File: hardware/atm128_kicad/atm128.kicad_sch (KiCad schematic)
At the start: 57 parts, among them J1 Power Jack, J2 Conn_02x16_Odd_Even, J3 Conn_02x16_Odd_Even, J4 ISP, J5 JTAG, J6 USB_B_Mini, U1 LM2596S-5, U2 ATmega128-16A, U3 CH340G, Y1 Crystal

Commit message: feat: update hw: USB_C, IDC ISP, CH340E
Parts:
- removed C10, C11, C14: 1uF, Capacitor_SMD:C_0805_2012Metric, symbol Device:C
- removed C12: 10nF, Capacitor_SMD:C_0805_2012Metric, symbol Device:C
- removed C13: 100nF, Capacitor_SMD:C_0805_2012Metric, symbol Device:C
- removed D8: RX, LED_SMD:LED_0805_2012Metric, symbol Device:LED
- removed J4: ISP, Connector_PinHeader_2.54mm:PinHeader_1x06_P2.54mm_Vertical, symbol Connector_Generic:Conn_01x06
- removed J6: USB_B_Mini, Connector_USB:USB_Micro-B_Molex-105017-0001, symbol Connector:USB_B_Mini
- removed R11, R14, R15: 1k, Resistor_SMD:R_0805_2012Metric, symbol Device:R
- removed TP3: 5V, TestPoint:TestPoint_Pad_D1.0mm, symbol Connector:TestPoint
- removed U3: CH340G, Package_SO:SOIC-16_3.9x9.9mm_P1.27mm, symbol Interface_USB:CH340G
- removed Y1: Crystal, Crystal:Crystal_SMD_5032-2Pin_5.0x3.2mm, symbol Device:Crystal
- added C15: 10nF, Capacitor_SMD:C_0805_2012Metric, symbol Device:C
- added C16: 1uF, Capacitor_SMD:C_0805_2012Metric, symbol Device:C
- added C17: 100nF, Capacitor_SMD:C_0805_2012Metric, symbol Device:C
- added J4: ISP, Connector_IDC:IDC-Header_2x05_P2.54mm_Vertical, symbol Connector:AVR-ISP-10
- added J6: USB_C_Receptacle_USB2.0, Connector_USB:USB_C_Receptacle_HRO_TYPE-C-31-M-12, symbol Connector:USB_C_Receptacle_USB2.0
- added R16, R17: 5.1k, Resistor_SMD:R_0805_2012Metric, symbol Device:R
- added R18, R19: 1k, Resistor_SMD:R_0805_2012Metric, symbol Device:R
- added U4: CH340E, Package_SO:MSOP-10_3x3mm_P0.5mm, symbol Interface_USB:CH340E
- D7: value TX -> PROG
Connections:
- net +5V: now also C16.2, J4.2 (VCC), J6.A4 (VBUS), J6.A9 (VBUS), J6.B4 (VBUS), J6.B9 (VBUS), U4.7 (VCC)
- net CH_RX: now also R19.2, U4.9 (RXD)
- net CH_TX: now also R18.2, U4.8 (TXD)
- net GND: now also C15.1, C16.1, J4.10 (GND), J4.4 (GND), J4.6 (GND), J4.8 (GND), J6.A1 (GND), J6.A12 (GND), J6.B1 (GND), J6.B12 (GND), J6.S1 (SHIELD), R16.2, R17.2, U4.3 (GND)
- net RXD0: now also J4.1 (MOSI)
- net RXD1: now also R18.1
- net SPI_SCK: now also J4.7 (SCK)
- net TXD0: now also J4.9 (MISO)
- net TXD1: now also R19.1
- net USB_D+: now also J6.A6 (D+), J6.B6 (D+), U4.1 (UD+)
- net USB_D-: now also J6.A7 (D-), J6.B7 (D-), U4.2 (UD-)
- net /reset renamed nRST
- net nRST: now also C17.2, J4.5 (~{RST})
- new net: C15.2, U4.10 (V3)
- new net: C17.1, U4.4 (~{RTS})
- new net: J6.B5 (CC2), R17.1
- new net: J6.A5 (CC1), R16.1
- no-connect marks 16 -> 13
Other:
- moved on the sheet: TP1, TP2, TP4, TP5

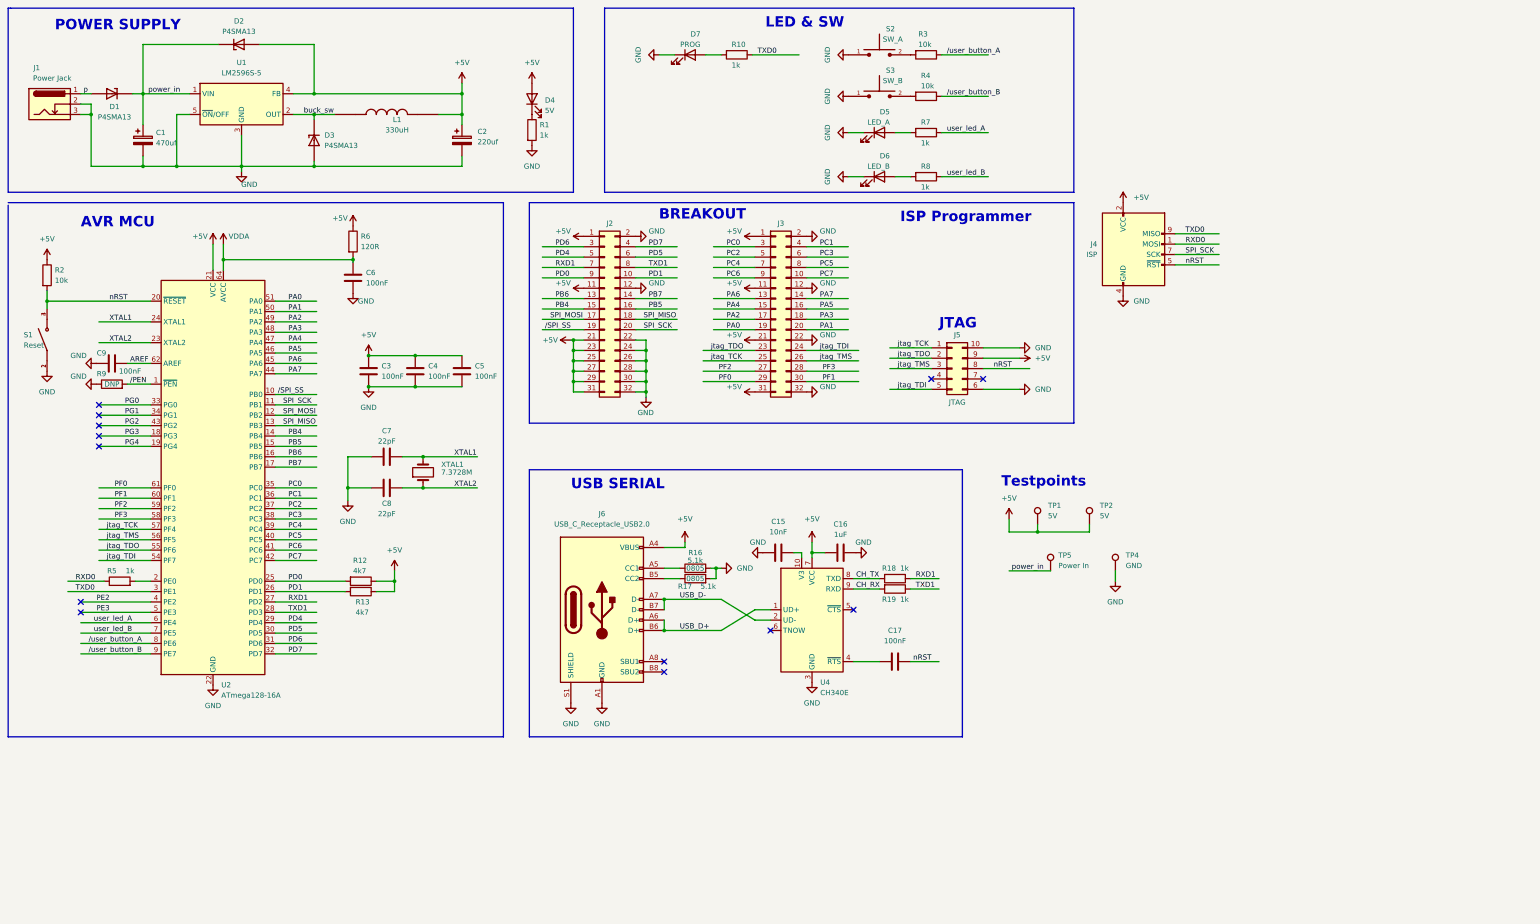
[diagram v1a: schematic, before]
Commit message: feat: update schematic Rev1.0
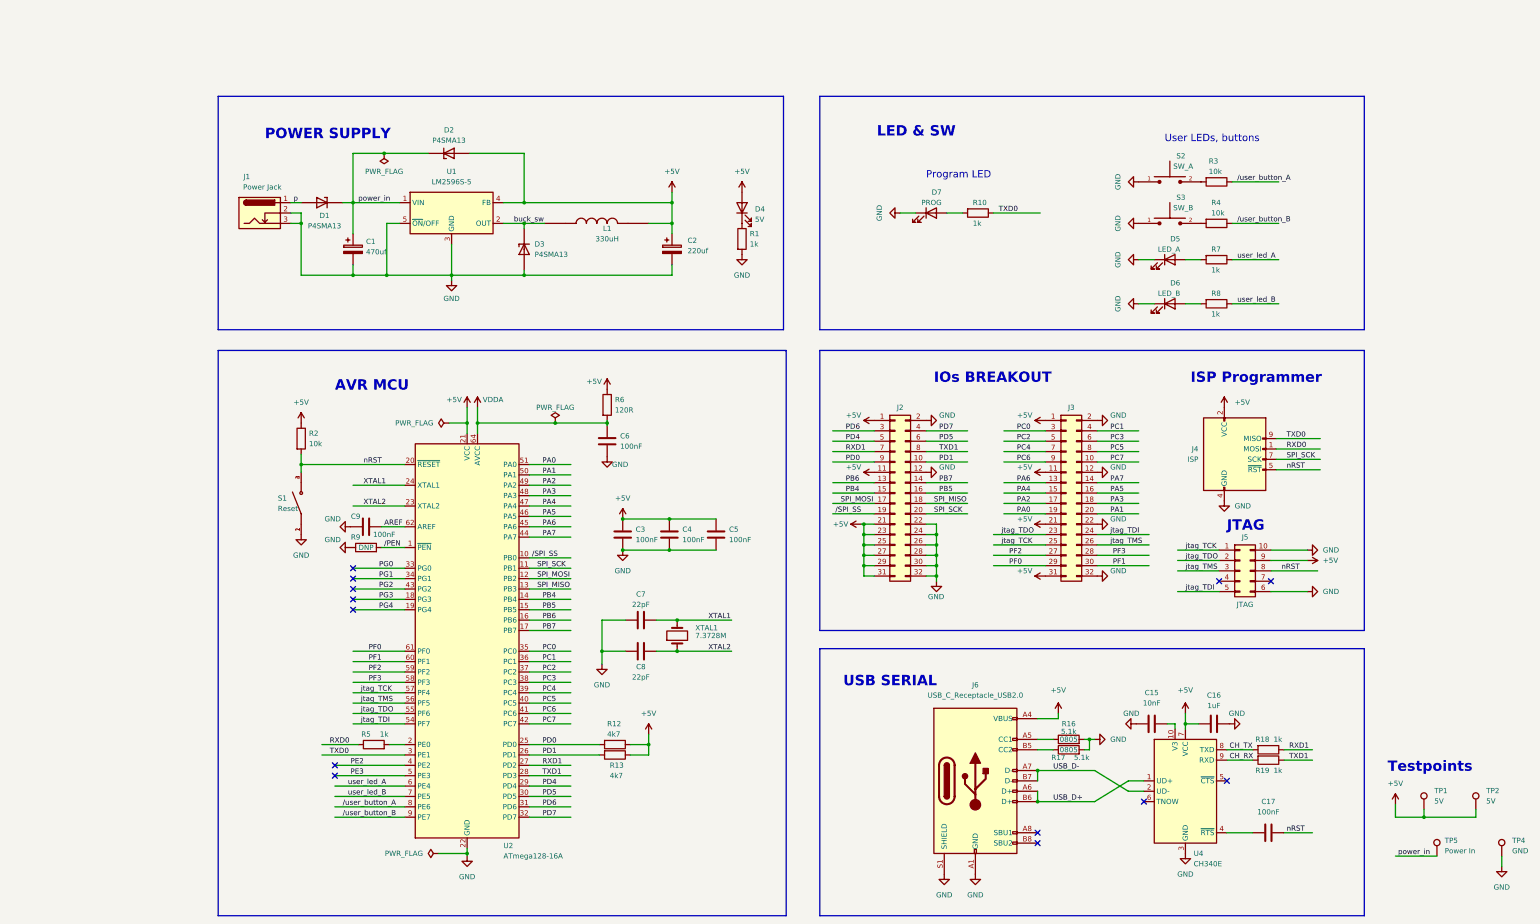
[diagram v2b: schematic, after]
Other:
- note added: "IOs BREAKOUT"
- note added: "Program LED"
- note added: "User LEDs, buttons"
- note removed: "BREAKOUT"
- moved on the sheet: C1, C15, C16, C17, C2, C3, C4, C5, C6, C7, C8, C9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

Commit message: feat: add TNOW LED, complete review for rev1.0
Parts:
- added D8: TNOW, LED_SMD:LED_0805_2012Metric, symbol Device:LED
- added R11: 1k, Resistor_SMD:R_0805_2012Metric, symbol Device:R
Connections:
- net GND: now also D8.1 (K)
- net tnow: now reaches U4.6 (TNOW)
- net tnow: now also R11.1
- new net: D8.2 (A), R11.2
- no-connect marks 13 -> 12
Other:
- note added: "UART1 Transmittion LED"
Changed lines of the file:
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@@
   )
   (no_connect (at 269.875 219.075))
-  (no_connect (at 295.91 208.915))
   (no_connect (at 102.235 159.385))
   (no_connect (at 102.235 161.925))
@@
     (stroke (width 0) (type default) (color 0 0 0 0))
   )
+  (wire (pts (xy 251.46 82.55) (xy 247.65 82.55))
+    (stroke (width 0) (type default) (color 0 0 0 0))
+  )
   (wire (pts (xy 94.615 197.485) (xy 114.935 197.485))
     (stroke (width 0) (type default) (color 0 0 0 0))
@@
     (stroke (width 0) (type default) (color 0 0 0 0))
   )
+  (wire (pts (xy 259.08 82.55) (xy 270.51 82.55))
+    (stroke (width 0) (type default) (color 0 0 0 0))
+  )
   (wire (pts (xy 102.235 184.785) (xy 114.935 184.785))
     (stroke (width 0) (type default) (color 0 0 0 0))
@@
     (stroke (width 0) (type default) (color 0 0 0 0))
   )
+  (wire (pts (xy 240.03 82.55) (xy 236.22 82.55))
+    (stroke (width 0) (type default) (color 0 0 0 0))
+  )
   (wire (pts (xy 357.505 209.55) (xy 357.505 212.725))
     (stroke (width 0) (type default) (color 0 0 0 0))
@@
     (stroke (width 0) (type default) (color 0 0 0 0))
   )
+  (wire (pts (xy 288.925 208.915) (xy 295.91 208.915))
+    (stroke (width 0) (type default) (color 0 0 0 0))
+  )
   (wire (pts (xy 259.08 64.77) (xy 270.51 64.77))
     (stroke (width 0) (type default) (color 0 0 0 0))
@@
     (effects (font (size 2.54 2.54) (thickness 0.254) bold) (justify left bottom))
   )
+  (text "UART1 Transmittion LED" (at 235.585 74.295 0)
+    (effects (font (size 1.778 1.778)) (justify left bottom))
+  )
   (text "Program LED" (at 242.57 56.515 0)
     (effects (font (size 1.778 1.778)) (justify left bottom))
@@
     (effects (font (size 1.27 1.27)) (justify left bottom))
   )
+  (label "tnow" (at 262.255 82.55 0)
+    (effects (font (size 1.27 1.27)) (justify left bottom))
+  )
   (label "USB_D-" (at 273.685 201.295 0)
     (effects (font (size 1.27 1.27)) (justify left bottom))
@@
     (effects (font (size 1.27 1.27)) (justify left bottom))
   )
+  (label "tnow" (at 290.195 208.915 0)
+    (effects (font (size 1.27 1.27)) (justify left bottom))
+  )
   (label "PC6" (at 148.59 187.325 0)
     (effects (font (size 1.27 1.27)) (justify left bottom))
@@
     (pin "1")
   )
+  (symbol (lib_id "power:GND") (at 236.22 82.55 270) (unit 1)
+    (in_bom yes) (on_board yes) (fields_autoplaced)
+    (property "Reference" "#PWR021" (id 0) (at 229.87 82.55 0)
+      (effects (font (size 1.27 1.27)) hide)
+    )
+    (property "Value" "GND" (id 1) (at 231.14 82.55 0))
+    (property "Footprint" "" (id 2) (at 236.22 82.55 0)
+      (effects (font (size 1.27 1.27)) hide)
+    )
+    (property "Datasheet" "" (id 3) (at 236.22 82.55 0)
+      (effects (font (size 1.27 1.27)) hide)
+    )
+    (pin "1")
+  )
   (symbol (lib_id "power:GND") (at 284.48 115.57 90) (unit 1)
     (in_bom yes) (on_board yes)
@@
     (pin "2")
   )
+  (symbol (lib_id "Device:LED") (at 243.84 82.55 0) (unit 1)
+    (in_bom yes) (on_board yes)
+    (property "Reference" "D8" (id 0) (at 246.38 77.47 0)
+      (effects (font (size 1.27 1.27)) (justify right))
+    )
+    (property "Value" "TNOW" (id 1) (at 246.38 80.01 0)
+      (effects (font (size 1.27 1.27)) (justify right))
+    )
+    (property "Footprint" "LED_SMD:LED_0805_2012Metric" (id 2) (at 243.84 82.55 0)
+      (effects (font (size 1.27 1.27)) hide)
+    )
+    (property "Datasheet" "~" (id 3) (at 243.84 82.55 0)
+      (effects (font (size 1.27 1.27)) hide)
+    )
+    (pin "1")
+    (pin "2")
+  )
   (symbol (lib_id "Device:R") (at 166.37 197.485 270) (unit 1)
     (in_bom yes) (on_board yes)
@@
     (pin "2")
   )
+  (symbol (lib_id "Device:R") (at 255.27 82.55 270) (unit 1)
+    (in_bom yes) (on_board yes)
+    (property "Reference" "R11" (id 0) (at 254 80.01 90)
+      (effects (font (size 1.27 1.27)) (justify left))
+    )
+    (property "Value" "1k" (id 1) (at 254 85.09 90)
+      (effects (font (size 1.27 1.27)) (justify left))
+    )
+    (property "Footprint" "Resistor_SMD:R_0805_2012Metric" (id 2) (at 255.27 80.772 90)
+      (effects (font (size 1.27 1.27)) hide)
+    )
+    (property "Datasheet" "~" (id 3) (at 255.27 82.55 0)
+      (effects (font (size 1.27 1.27)) hide)
+    )
+    (pin "1")
+    (pin "2")
+  )
   (symbol (lib_id "SW1437565-9:4-1437565-9") (at 89.535 135.89 90) (unit 1)
     (in_bom yes) (on_board yes)
@@
       (reference "#PWR020") (unit 1) (value "GND") (footprint "")
     )
+    (path "/2cdbb47e-02b8-421a-9128-6cd2fa45afe8"
+      (reference "#PWR021") (unit 1) (value "GND") (footprint "")
+    )
     (path "/0e00c69d-c672-4ed4-8e5f-24d8dda16db9"
       (reference "#PWR022") (unit 1) (value "+5V") (footprint "")
@@
       (reference "D7") (unit 1) (value "PROG") (footprint "LED_SMD:LED_0805_2012Metric")
     )
+    (path "/7ccec5d7-bfd4-44c4-ac09-e56d40d97de7"
+      (reference "D8") (unit 1) (value "TNOW") (footprint "LED_SMD:LED_0805_2012Metric")
+    )
     (path "/1cd5c61e-fddd-4443-a1c5-362a48bac817"
       (reference "J1") (unit 1) (value "Power Jack") (footprint "Connector_BarrelJack:BarrelJack_GCT_DCJ200-10-A_Horizontal")
@@
       (reference "R10") (unit 1) (value "1k") (footprint "Resistor_SMD:R_0805_2012Metric")
     )
+    (path "/9b9c41b5-5098-480e-a6ee-aceee0445c49"
+      (reference "R11") (unit 1) (value "1k") (footprint "Resistor_SMD:R_0805_2012Metric")
+    )
     (path "/e8b26f23-8187-49ed-a173-deefb016a1ea"
